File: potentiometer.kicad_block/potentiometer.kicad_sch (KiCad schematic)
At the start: 1 part

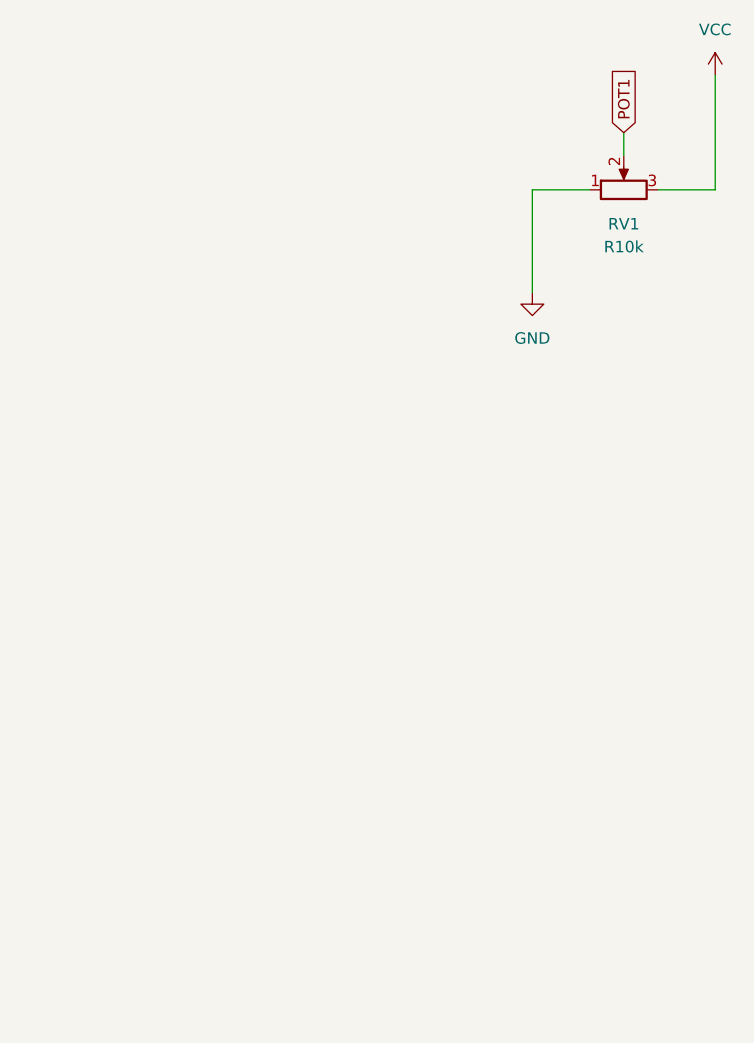
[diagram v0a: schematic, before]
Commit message: added optional filtering capacitor to potentiometer schematic block
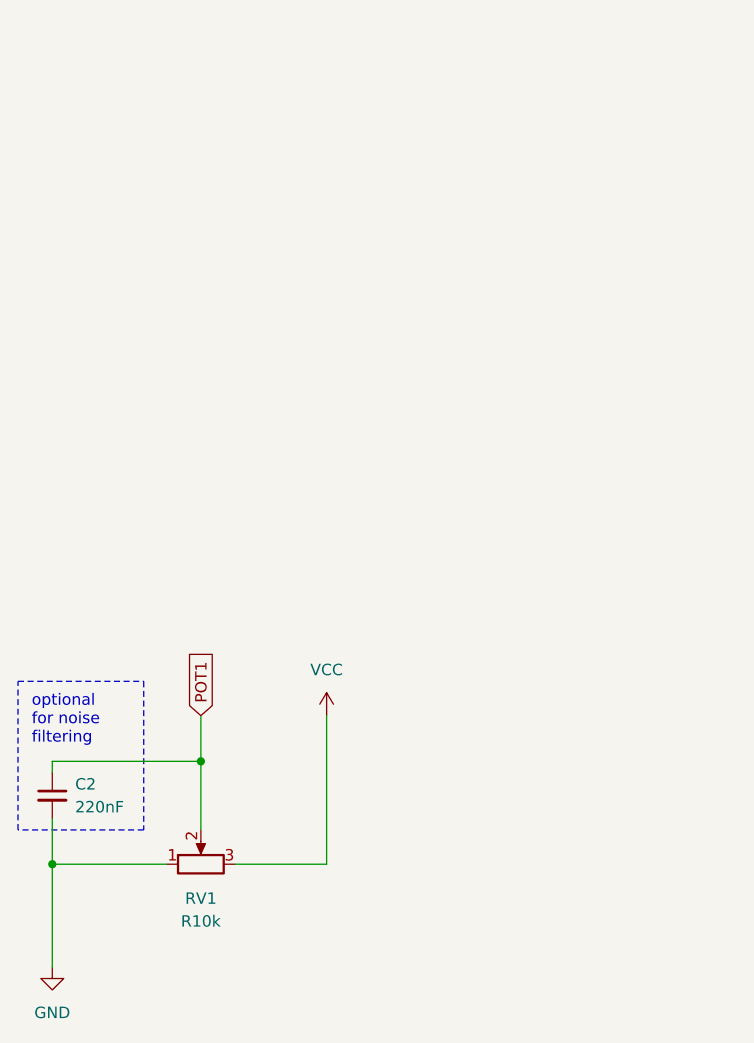
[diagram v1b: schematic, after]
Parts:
- added C2: 220nF, Capacitor_THT:C_Disc_D7.0mm_W2.5mm_P5.00mm, symbol Device:C_Small
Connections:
- net GND: now also C2.2
- net POT1: now also C2.1
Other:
- note added: "optional for noise filtering"
